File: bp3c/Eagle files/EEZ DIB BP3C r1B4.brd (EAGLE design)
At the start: 110 x 85 mm, 30 parts, among them Q1 IRLML6244TRPBF, Q2 IRLML6244TRPBF, X1 ZL202-20G, X2 ZL202-20G, X3 ZL202-20G, X4 ZL212-40KG, X5 TSW-113-07-F-D, X6 TSW-113-07-F-D, X7 TSW-113-07-F-D

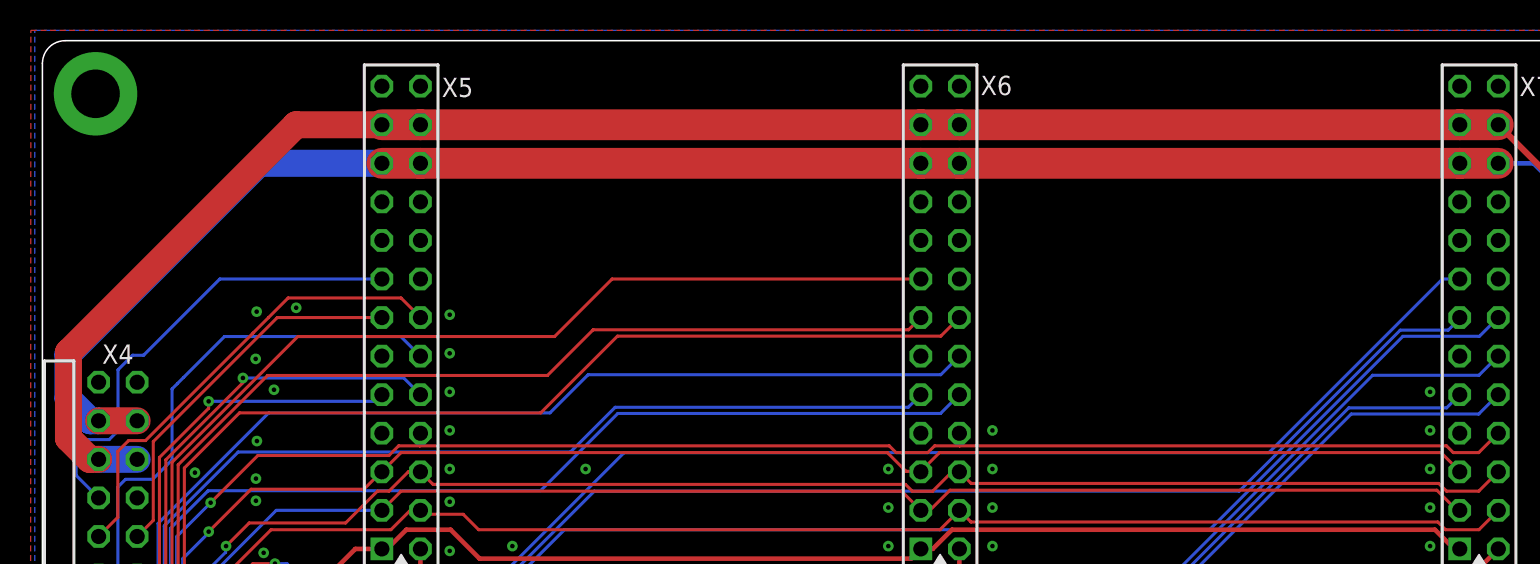
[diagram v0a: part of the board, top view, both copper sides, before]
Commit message: BP3C module addressing fix
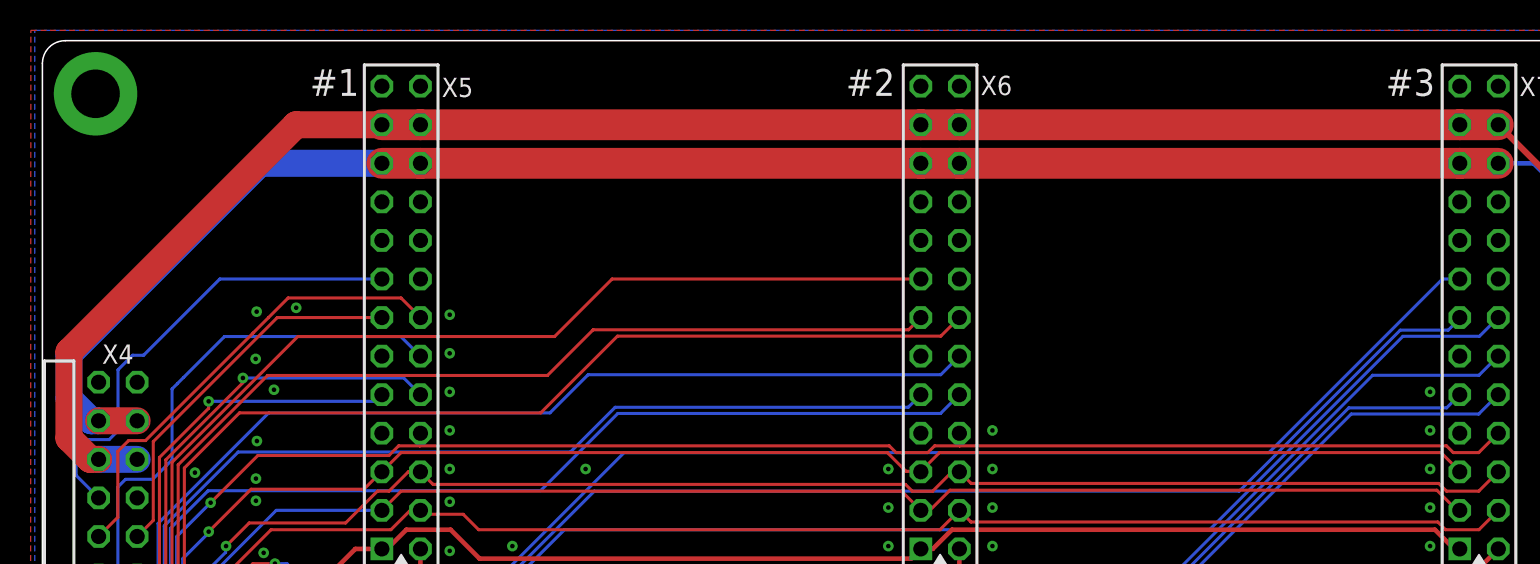
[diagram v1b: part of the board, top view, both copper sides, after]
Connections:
- net GND: now also X6.19, X7.17, X7.19; no longer X6.17, X6.18, X7.18
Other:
- board text added: "#1"
- board text added: "#2"
- board text added: "#3"
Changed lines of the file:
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@@
 <setting verticaltext="up"/>
 </settings>
-<grid distance="10" unitdist="mm" unit="mm" style="lines" multiple="10" display="no" altdistance="12.5" altunitdist="mil" altunit="mil"/>
+<grid distance="2.5" unitdist="mil" unit="mil" style="lines" multiple="10" display="no" altdistance="12.5" altunitdist="mil" altunit="mil"/>
 <layers>
 <layer number="1" name="Top" color="11" fill="1" visible="yes" active="yes"/>
@@
 <layer number="17" name="Pads" color="6" fill="1" visible="yes" active="yes"/>
 <layer number="18" name="Vias" color="6" fill="1" visible="yes" active="yes"/>
-<layer number="19" name="Unrouted" color="6" fill="1" visible="no" active="yes"/>
+<layer number="19" name="Unrouted" color="6" fill="1" visible="yes" active="yes"/>
 <layer number="20" name="Dimension" color="12" fill="1" visible="yes" active="yes"/>
 <layer number="21" name="tPlace" color="7" fill="1" visible="yes" active="yes"/>
@@
 <dimension x1="82" y1="42.5" x2="78.5" y2="87" x3="91.5" y3="64.75" textsize="1.778" layer="47" dtype="vertical"/>
 <dimension x1="83.4" y1="2.1" x2="84.5" y2="19.6" x3="79.6" y3="10.85" textsize="1.778" layer="47" dtype="vertical"/>
+<text x="7.62" y="86.36" size="1.778" layer="21" ratio="10">#1</text>
+<text x="42.926" y="86.36" size="1.778" layer="21" ratio="10">#2</text>
+<text x="78.486" y="86.36" size="1.778" layer="21" ratio="10">#3</text>
 </plain>
 <attributes>
@@
 <contactref element="X7" pad="25"/>
 <contactref element="X7" pad="16"/>
-<contactref element="X7" pad="18"/>
 <contactref element="X7" pad="26"/>
 <contactref element="X6" pad="7"/>
 <contactref element="X6" pad="11"/>
 <contactref element="X6" pad="16"/>
-<contactref element="X6" pad="18"/>
 <contactref element="X6" pad="25"/>
 <contactref element="X6" pad="26"/>
@@
 <contactref element="X5" pad="26"/>
 <contactref element="X5" pad="16"/>
-<contactref element="X6" pad="17"/>
 <via x="81.407" y="56.7055" extent="1-16" drill="0.3" shape="octagon"/>
 <via x="52.578" y="61.7855" extent="1-16" drill="0.3" shape="octagon"/>
@@
 <via x="1.5875" y="22.1615" extent="1-16" drill="0.3" shape="octagon"/>
 <via x="1.143" y="52.578" extent="1-16" drill="0.3" shape="octagon"/>
+<contactref element="X6" pad="19"/>
+<contactref element="X7" pad="17"/>
+<contactref element="X7" pad="19"/>
 </signal>
 <signal name="+5V">
@@
 <contactref element="X4" pad="36"/>
 <wire x1="88.9" y1="81.46" x2="88.9" y2="81.28" width="0.4064" layer="1"/>
-<wire x1="-6.3" y1="62.42" x2="-6.896" y2="62.42" width="1.778" layer="1"/>
-<wire x1="-6.896" y1="62.42" x2="-8.2855" y2="63.8095" width="1.778" layer="1"/>
-<wire x1="-8.2855" y1="63.8095" x2="-8.2855" y2="69.469" width="1.778" layer="1"/>
+<wire x1="-8.255" y1="63.8175" x2="-8.255" y2="69.4995" width="1.778" layer="1"/>
 <wire x1="-3.76" y1="62.42" x2="-6.3" y2="62.42" width="1.778" layer="16"/>
 <contactref element="X7" pad="23"/>
@@
 <wire x1="95.885" y1="17.653" x2="88.9" y2="17.653" width="0.3048" layer="1"/>
 <wire x1="12.36" y1="84.46" x2="6.7055" y2="84.46" width="1.778" layer="1"/>
-<wire x1="6.7055" y1="84.46" x2="-8.2855" y2="69.469" width="1.778" layer="1"/>
-<wire x1="47.625" y1="10.541" x2="47.6377" y2="10.5537" width="0" layer="19" extent="16-16"/>
+<wire x1="-8.255" y1="69.4995" x2="6.7055" y2="84.46" width="1.778" layer="1"/>
+<wire x1="-6.3" y1="62.42" x2="-6.8575" y2="62.42" width="1.778" layer="1"/>
+<wire x1="-6.8575" y1="62.42" x2="-8.255" y2="63.8175" width="1.778" layer="1"/>
+<wire x1="47.625" y1="10.541" x2="47.6377" y2="10.5537" width="0" layer="19" extent="1-16"/>
 </signal>
 <signal name="N$7">
@@
 <wire x1="85.9" y1="81.92" x2="88.2219" y2="81.92" width="0.3048" layer="16"/>
 <wire x1="88.2219" y1="81.92" x2="90.5637" y2="79.5782" width="0.3048" layer="16"/>
-<wire x1="12.36" y1="81.92" x2="4.2595" y2="81.92" width="1.778" layer="16"/>
-<wire x1="4.2595" y1="81.92" x2="-8.3185" y2="69.342" width="1.778" layer="16"/>
-<wire x1="-8.3185" y1="69.342" x2="-8.3185" y2="66.421" width="1.778" layer="16"/>
-<wire x1="-8.3185" y1="66.421" x2="-6.8575" y2="64.96" width="1.778" layer="16"/>
-<wire x1="-6.3" y1="64.96" x2="-6.8575" y2="64.96" width="1.778" layer="16"/>
+<wire x1="-8.255" y1="69.342" x2="-8.255" y2="66.421" width="1.778" layer="16"/>
+<wire x1="12.36" y1="81.92" x2="4.323" y2="81.92" width="1.778" layer="16"/>
+<wire x1="4.323" y1="81.92" x2="-8.255" y2="69.342" width="1.778" layer="16"/>
+<wire x1="-6.3" y1="64.96" x2="-6.794" y2="64.96" width="1.778" layer="16"/>
+<wire x1="-6.794" y1="64.96" x2="-8.255" y2="66.421" width="1.778" layer="16"/>
 </signal>
 <signal name="N$3">
